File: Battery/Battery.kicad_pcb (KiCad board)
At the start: 2 copper layers, 27.9 x 30.5 mm, 6 parts, among them J1 Conn_01x06, Q1 BSS138, SW1 SW_SPDT, SW2 SW_SPDT

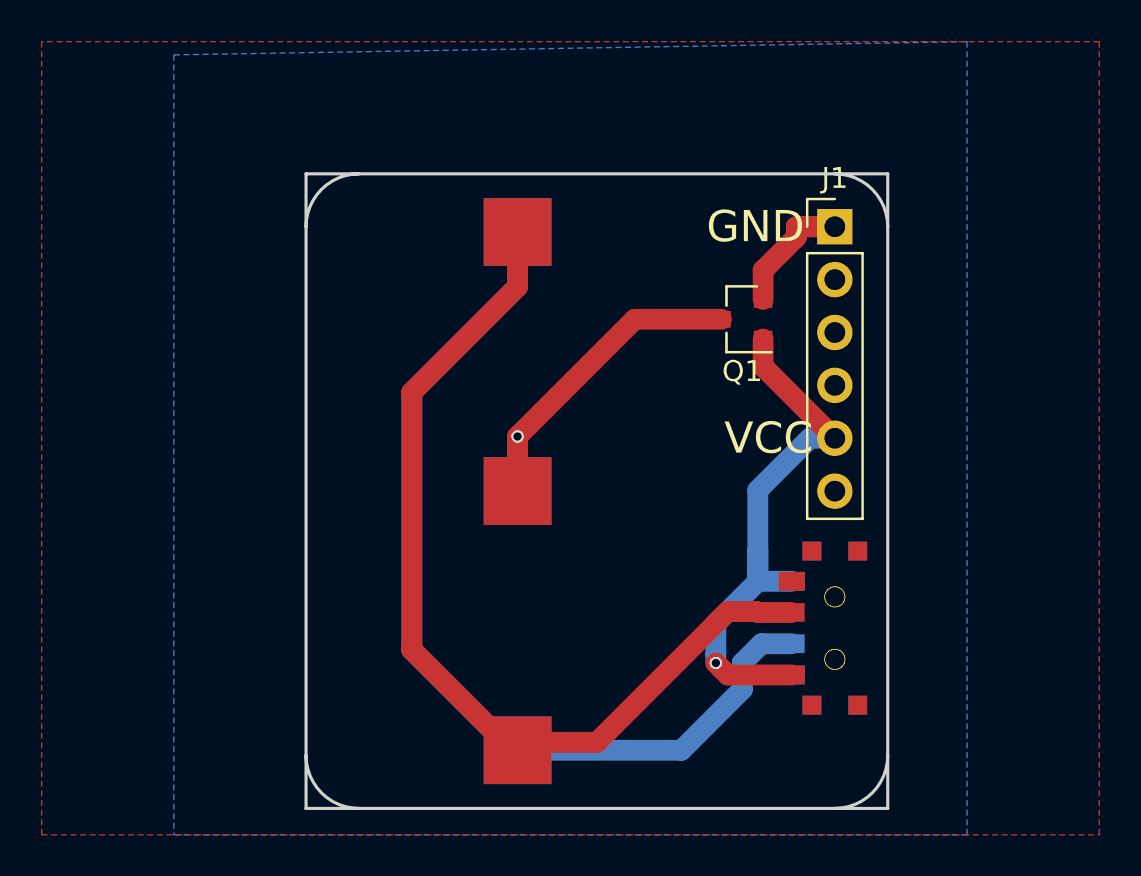
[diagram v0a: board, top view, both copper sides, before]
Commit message: updating to V1.1 - segregating GPIO from Serial
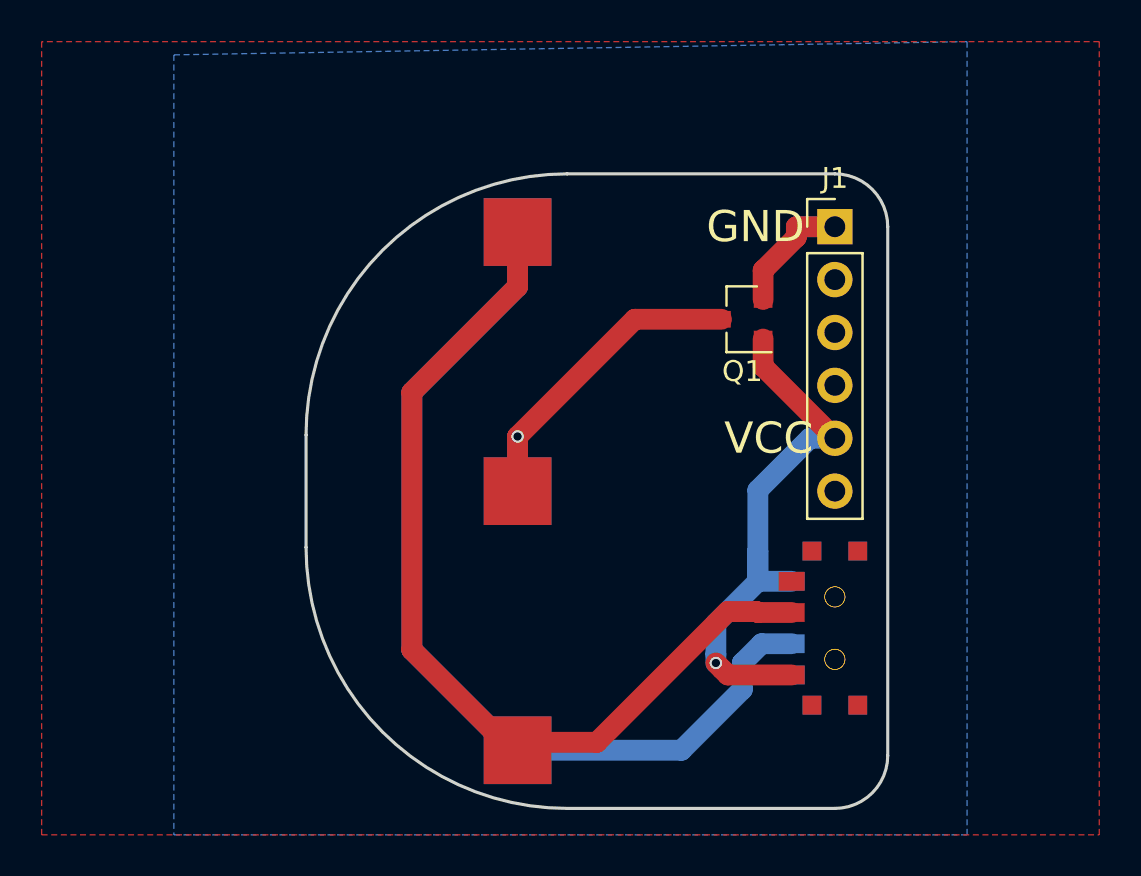
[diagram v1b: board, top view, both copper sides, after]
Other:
- outline, holes or cut-outs redrawn
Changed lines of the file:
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@@
   )
   (setup
-    (last_trace_width 1)
+    (last_trace_width 0.25)
     (user_trace_width 1)
     (trace_clearance 0.2)
@@
   )
   (gr_arc (start 177.8 104.14) (end 177.8 101.6) (angle 90) (layer Edge.Cuts) (width 0.15))
-  (gr_arc (start 154.94 104.14) (end 152.4 104.14) (angle 90) (layer Edge.Cuts) (width 0.15))
-  (gr_arc (start 154.94 129.54) (end 154.94 132.08) (angle 90) (layer Edge.Cuts) (width 0.15))
+  (gr_arc (start 164.94 114.14) (end 152.4 114.14) (angle 90) (layer Edge.Cuts) (width 0.15))
+  (gr_arc (start 164.94 119.54) (end 164.94 132.08) (angle 90) (layer Edge.Cuts) (width 0.15))
   (gr_arc (start 177.8 129.54) (end 180.34 129.54) (angle 90) (layer Edge.Cuts) (width 0.15))
-  (gr_line (start 152.4 101.6) (end 180.34 101.6) (layer Edge.Cuts) (width 0.15))
-  (gr_line (start 152.4 132.08) (end 152.4 101.6) (layer Edge.Cuts) (width 0.15))
-  (gr_line (start 180.34 132.08) (end 152.4 132.08) (layer Edge.Cuts) (width 0.15))
-  (gr_line (start 180.34 101.6) (end 180.34 132.08) (layer Edge.Cuts) (width 0.15))
+  (gr_line (start 164.9476 101.6) (end 177.8 101.6) (layer Edge.Cuts) (width 0.15))
+  (gr_line (start 152.4 119.5324) (end 152.4 114.1476) (layer Edge.Cuts) (width 0.15))
+  (gr_line (start 177.8 132.08) (end 164.9476 132.08) (layer Edge.Cuts) (width 0.15))
+  (gr_line (start 180.34 104.14) (end 180.34 129.54) (layer Edge.Cuts) (width 0.15))
   (segment (start 162.56 128.905) (end 166.37 128.905) (width 1) (layer F.Cu) (net 1))
   (segment (start 166.37 128.905) (end 172.650011 122.624989) (width 1) (layer F.Cu) (net 1))
